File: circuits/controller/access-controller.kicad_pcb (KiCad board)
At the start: 4 copper layers, 150 x 90 mm, 144 parts, among them J1 Conn_01x01_Female, J10 Terminal_01x03, J11 Terminal_01x04, J12 Screw_Terminal_01x05, J13 Conn_02x06_Odd_Even, J14 Terminal_01x04, J15 Terminal_01x03, J16 Terminal_01x03, J17 Terminal_01x03, J18 Terminal_01x04, J19 Screw_Terminal_01x05, J2 Conn_01x01_Female, J20 USB_MINI_B, J21 USB_MINI_B, J23 CONN_RJ45, J3 Conn_01x01_Female, J4 Conn_01x01_Female, J5 Barrel_Jack_Switch, J6 Screw_Terminal_01x02, J7 Terminal_01x04, J8 Terminal_01x03, J9 Terminal_01x03, Q1 Q_L8050QLT1G, Q10 Q_MMBT5551, Q11 Q_MMBT5551, Q12 Q_MMBT5551, Q13 Q_MMBT5551, Q14 Q_MMBT5551, Q15 Q_MMBT5551, Q2 Q_L8550HQLT1G, Q3 Q_MMBT5551, Q6 Q_MMBT5551, Q7 Q_MMBT5551, Q8 Q_AO3400A, Q9 Q_AO3400A, U1 MCP23017_SS, U10 TLP291-4, U12 W5500, U3 REG_AMS1117-3.3, U4 MIC29302WU, U5 TLP291-4, U6 CP2102N-Axx-xQFN28, U7 ESP32-S3-WROOM-1, U8 REG_MT2492, U9 TLP291-4

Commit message: testing radar
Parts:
- added D13: White, LED_SMD:LED_0603_1608Metric_Pad1.05x0.95mm_HandSolder, F.Cu at (190.3, 119.2)
- added D18: White, LED_SMD:LED_0603_1608Metric_Pad1.05x0.95mm_HandSolder, F.Cu at (199.7, 60.4)
- added D19: White, LED_SMD:LED_0603_1608Metric_Pad1.05x0.95mm_HandSolder, F.Cu at (213.2, 119.8)
- added D2: White, LED_SMD:LED_0603_1608Metric_Pad1.05x0.95mm_HandSolder, F.Cu at (99.0, 129.8)
- added D20: White, LED_SMD:LED_0603_1608Metric_Pad1.05x0.95mm_HandSolder, F.Cu at (180.2, 59.5)
- added D21: White, LED_SMD:LED_0603_1608Metric_Pad1.05x0.95mm_HandSolder, F.Cu at (174.6, 119.8)
- added D22: White, LED_SMD:LED_0603_1608Metric_Pad1.05x0.95mm_HandSolder, F.Cu at (155.8, 120.2)
- added D23: White, LED_SMD:LED_0603_1608Metric_Pad1.05x0.95mm_HandSolder, F.Cu at (135.0, 117.9)
- added D24: White, LED_SMD:LED_0603_1608Metric_Pad1.05x0.95mm_HandSolder, F.Cu at (202.3, 111.6)
- added D25: White, LED_SMD:LED_0603_1608Metric_Pad1.05x0.95mm_HandSolder, F.Cu at (135.2, 115.8)
- added D26: White, LED_SMD:LED_0603_1608Metric_Pad1.05x0.95mm_HandSolder, F.Cu at (202.4, 72.1)
- added D27: White, LED_SMD:LED_0603_1608Metric_Pad1.05x0.95mm_HandSolder, F.Cu at (160.9, 59.3)
- added D28: White, LED_SMD:LED_0603_1608Metric_Pad1.05x0.95mm_HandSolder, F.Cu at (143.6, 59.3)
- added D29: White, LED_SMD:LED_0603_1608Metric_Pad1.05x0.95mm_HandSolder, F.Cu at (202.2, 107.4)
- added D30: White, LED_SMD:LED_0603_1608Metric_Pad1.05x0.95mm_HandSolder, F.Cu at (202.4, 68.3)
- added D31: White, LED_SMD:LED_0603_1608Metric_Pad1.05x0.95mm_HandSolder, F.Cu at (135.1, 113.2)
- added D32: White, LED_SMD:LED_0603_1608Metric_Pad1.05x0.95mm_HandSolder, F.Cu at (119.5, 60.6)
- added D33: White, LED_SMD:LED_0603_1608Metric_Pad1.05x0.95mm_HandSolder, F.Cu at (119.5, 62.7)
- added D34: White, LED_SMD:LED_0603_1608Metric_Pad1.05x0.95mm_HandSolder, F.Cu at (119.5, 64.9)
- added R1: 10K, Resistor_SMD:R_0402_1005Metric_Pad0.72x0.64mm_HandSolder, F.Cu at (97.4, 130.4)
- added R2: 10K, Resistor_SMD:R_0402_1005Metric_Pad0.72x0.64mm_HandSolder, F.Cu at (190.8, 117.5)
- added R3: 10K, Resistor_SMD:R_0402_1005Metric_Pad0.72x0.64mm_HandSolder, F.Cu at (199.2, 62.1)
- added R32: 10K, Resistor_SMD:R_0402_1005Metric_Pad0.72x0.64mm_HandSolder, F.Cu at (175.2, 118.2)
- added R33: 10K, Resistor_SMD:R_0402_1005Metric_Pad0.72x0.64mm_HandSolder, F.Cu at (156.4, 118.5)
- added R34: 10K, Resistor_SMD:R_0402_1005Metric_Pad0.72x0.64mm_HandSolder, F.Cu at (138.1, 118.2)
- added R35: 10K, Resistor_SMD:R_0402_1005Metric_Pad0.72x0.64mm_HandSolder, F.Cu at (200.8, 112.1)
- added R36: 10K, Resistor_SMD:R_0402_1005Metric_Pad0.72x0.64mm_HandSolder, F.Cu at (138.2, 116.0)
- added R4: 10K, Resistor_SMD:R_0402_1005Metric_Pad0.72x0.64mm_HandSolder, F.Cu at (213.8, 118.2)
- added R5: 10K, Resistor_SMD:R_0402_1005Metric_Pad0.72x0.64mm_HandSolder, F.Cu at (180.8, 61.2)
- added R74: 10K, Resistor_SMD:R_0402_1005Metric_Pad0.72x0.64mm_HandSolder, F.Cu at (200.8, 72.8)
- added R75: 10K, Resistor_SMD:R_0402_1005Metric_Pad0.72x0.64mm_HandSolder, F.Cu at (161.6, 61.0)
- added R76: 10K, Resistor_SMD:R_0402_1005Metric_Pad0.72x0.64mm_HandSolder, F.Cu at (144.1, 61.0)
- added R77: 10K, Resistor_SMD:R_0402_1005Metric_Pad0.72x0.64mm_HandSolder, F.Cu at (200.7, 106.8)
- added R78: 10K, Resistor_SMD:R_0402_1005Metric_Pad0.72x0.64mm_HandSolder, F.Cu at (200.7, 67.8)
- added R79: 10K, Resistor_SMD:R_0402_1005Metric_Pad0.72x0.64mm_HandSolder, F.Cu at (138.2, 113.0)
- added R80: 10K, Resistor_SMD:R_0402_1005Metric_Pad0.72x0.64mm_HandSolder, F.Cu at (116.5, 60.5)
- added R81: 10K, Resistor_SMD:R_0402_1005Metric_Pad0.72x0.64mm_HandSolder, F.Cu at (116.5, 62.4)
- added R82: 10K, Resistor_SMD:R_0402_1005Metric_Pad0.72x0.64mm_HandSolder, F.Cu at (116.4, 64.7)
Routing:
- net /POWER: track 55.5 -> 92.9 mm, vias 9 -> 12
- net /LOCK0_OUT: track 11.6 -> 31.5 mm, vias 0 -> 2
- net /LOCK0_CLOSE: track 45.8 -> 62.9 mm, vias 2 -> 3
- net /LOCK0_STATE: track 45.9 -> 62.6 mm, vias 0 -> 1
- net /LOCK1_CLOSE: track 70.0 -> 86.7 mm, vias 4 -> 5
- net /LOCK1_STATE: track 77.7 -> 93.3 mm
- net /MOTION1: track 16.9 -> 29.6 mm
- net /WG0_DATA0: track 15.3 -> 27.4 mm, vias 0 -> 2
- net /KEYPAD1: track 58.0 -> 69.9 mm, vias 0 -> 1
- net /LOCK1_OUT: track 13.6 -> 24.9 mm, vias 0 -> 2
- net /KEYPAD0: track 25.2 -> 36.2 mm
- net /EXIT1: track 39.9 -> 50.5 mm
- net /WG0_DATA1: track 26.0 -> 36.5 mm, vias 0 -> 2
- net /MOTION0: track 28.0 -> 37.6 mm
- net /WG1_DATA1: track 14.5 -> 24.0 mm, vias 0 -> 2
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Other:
- board text added: "ACCESS CONTROLLER v0.7 BY ANDY PAYNE"
- board text removed: "ACCESS CONTROLLER v0.6"

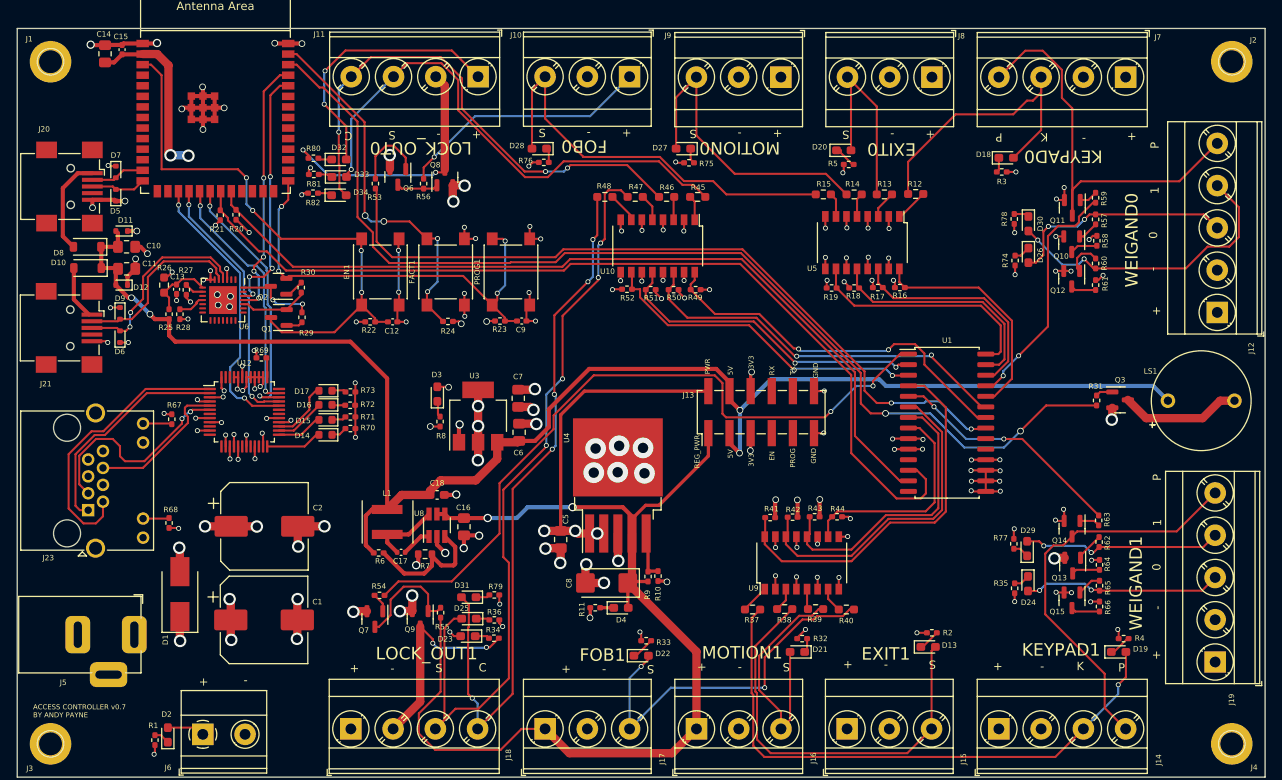
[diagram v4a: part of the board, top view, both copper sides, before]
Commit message: Remove obsolete access controller lock file and multiple outdated backup zip files. Enhance automation service with improved logging, including a shutdown handler and better memory management for log persistence. Introduce new API routes for Wiegand state management and update related services for improved functionality and error handling.
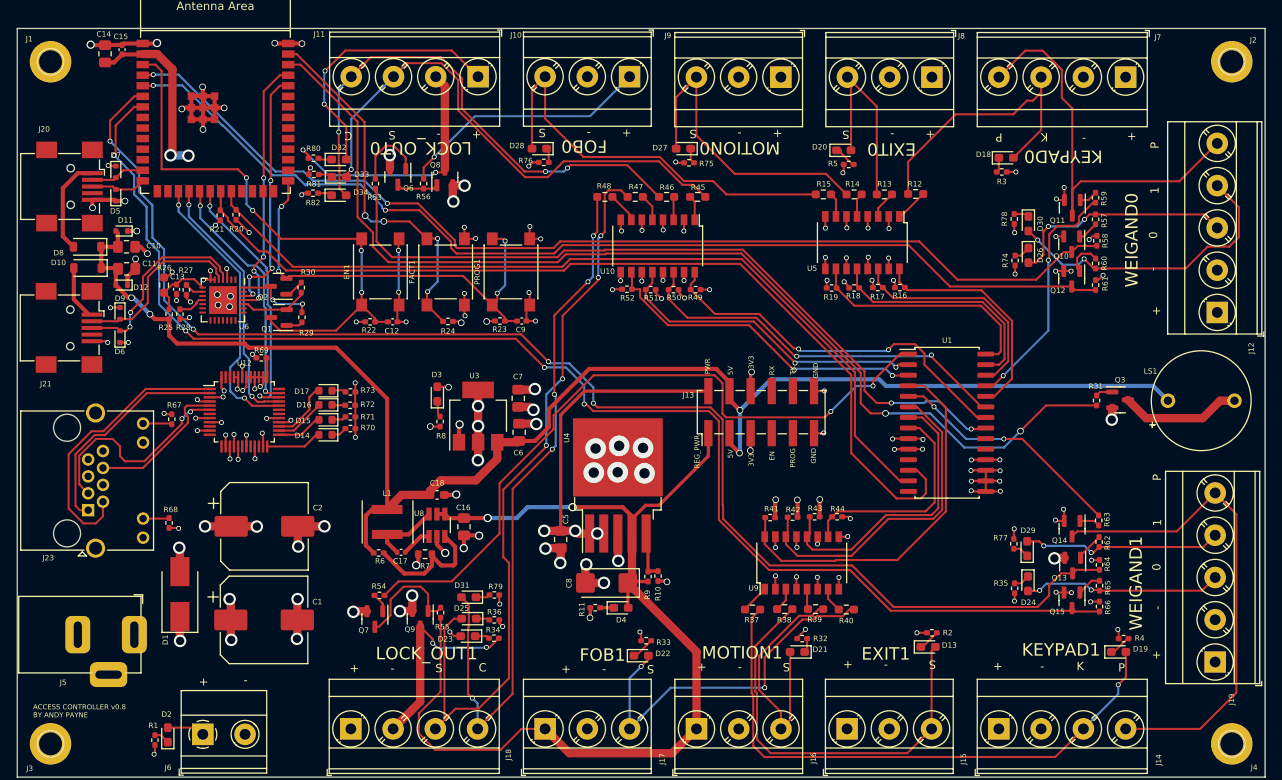
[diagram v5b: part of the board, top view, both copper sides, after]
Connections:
- U7 pad 4: /Microcontroller/IO4 -> /WG0_DATA_SENSE0
- U7 pad 5: /Microcontroller/IO5 -> /WG0_DATA_SENSE1
- U7 pad 6: /Microcontroller/IO6 -> /WG1_DATA_SENSE0
- U7 pad 7: /Microcontroller/IO7 -> /WG1_DATA_SENSE1
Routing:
- net /WG1_DATA_SENSE0: track 3.41 -> 167.8 mm, vias 0 -> 4
- net /WG1_DATA_SENSE1: track 3.48 -> 164.8 mm, vias 0 -> 4
- net /WG0_DATA_SENSE0: track 3.18 -> 127.5 mm, vias 0 -> 2
- net /WG0_DATA_SENSE1: track 3.05 -> 126.2 mm, vias 0 -> 2
- net /PUSH1: track 48.5 -> 59.5 mm
- net /5V: track 186.3 -> 184.9 mm
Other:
- board text added: "ACCESS CONTROLLER v0.8 BY ANDY PAYNE"
- board text removed: "ACCESS CONTROLLER v0.7 BY ANDY PAYNE"

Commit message: order from fab
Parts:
- added J22: RF_MODULE, Library:RXB6_RF_MODULE, F.Cu at (142.0, 83.7)
- added Q4: Q_MMBT5551, Package_TO_SOT_SMD:SOT-23, F.Cu at (126.3, 88.5)
- added R83: 10K, Resistor_SMD:R_0402_1005Metric_Pad0.72x0.64mm_HandSolder, F.Cu at (124.8, 86.0)
- added R84: 10K, Resistor_SMD:R_0402_1005Metric_Pad0.72x0.64mm_HandSolder, F.Cu at (127.3, 86.0)
- moved J13 0.29 mm to (170.2, 91.2)
- moved R79 0.10 mm to (138.3, 113.0)
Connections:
- U7 pad 8: /Microcontroller/IO15 -> /DATA_IO
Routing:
- net /DATA_IO: track 0.00 -> 66.3 mm, vias 0 -> 2
- net /5V: track 184.9 -> 203.7 mm
- net /DATA: track 0.00 -> 2.62 mm
- net /ANTENNA: track 0.00 -> 2.54 mm
- net Net-(Q4-B): track 0.00 -> 2.01 mm
- net /3V3: track 89.0 -> 89.9 mm, vias 47 -> 48
- net GND: track 238.4 -> 238.9 mm, vias 145 -> 146
